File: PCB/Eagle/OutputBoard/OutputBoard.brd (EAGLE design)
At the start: 100 x 80 mm, 10 parts, among them IC1 74LS138N

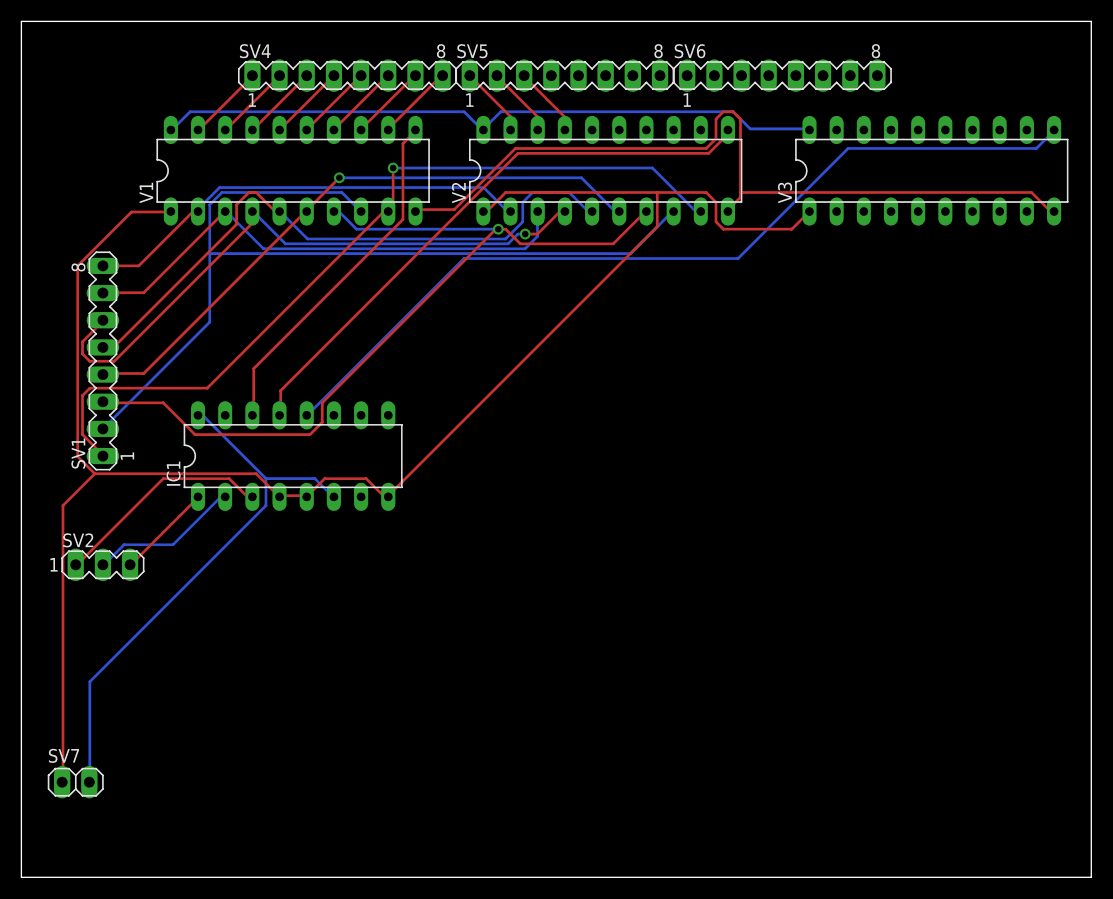
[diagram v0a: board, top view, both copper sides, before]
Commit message: Blank display for IAS and updates in PCB boards
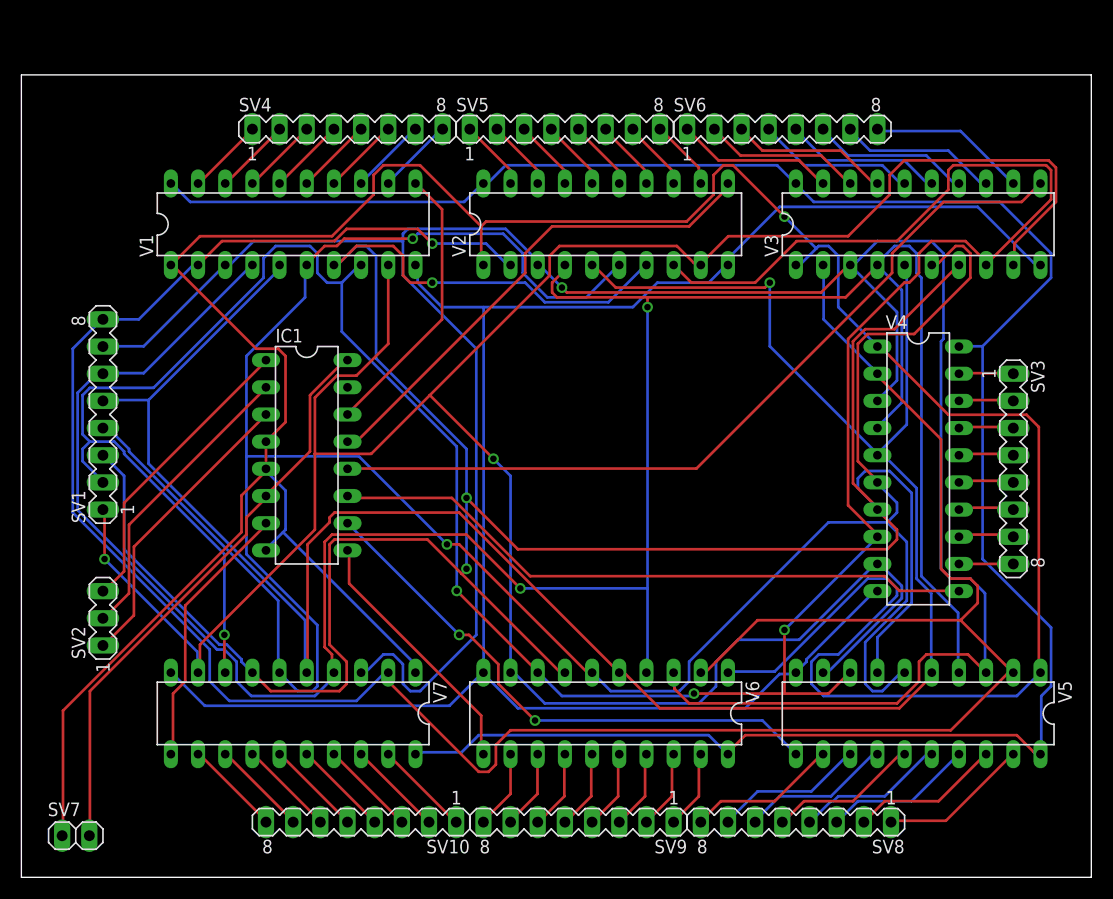
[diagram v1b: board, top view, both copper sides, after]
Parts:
- added SV10, SV3, SV8, SV9: (no value), con-lstb:MA08-1
- added V4, V5, V6, V7: 74574N, 74ttl-din:DIL20
- moved V3 5.16 mm to (83.8, 61.0)
- moved V1 5.00 mm to (25.4, 61.0)
- moved V2 5.00 mm to (54.6, 61.0)
- moved SV1 5.00 mm to (7.62, 43.3)
- moved SV2 5.00 mm to (7.62, 24.2), turned to 90 degrees
- moved SV4 5.00 mm to (30.5, 69.9)
- moved SV5 5.00 mm to (50.8, 69.9)
- moved SV6 5.00 mm to (71.1, 69.9)
- moved SV7 5.00 mm to (5.08, 3.89)
- moved IC1 1.27 mm to (26.7, 39.5), turned to 270 degrees
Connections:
- removed net BUS0: SV1.8, V1.2, V2.2
- removed net DATA4: SV1.4, V1.6, V2.6
- removed net DATA5: SV1.3, V1.7, V2.7
- removed net DATA6: SV1.2, V1.8, V2.8
- removed net DATA7: SV1.1, V1.9, V2.9
- removed net N$13: SV1.7, V1.3, V2.3
- removed net N$14: SV1.6, V1.4, V2.4
- removed net N$15: SV1.5, V1.5, V2.5
- new net BUS1: SV1.8, V1.2, V2.2, V3.2, V4.2, V5.2, V6.2, V7.2
- new net DATA1: SV1.1, V1.9, V2.9, V3.9, V4.9, V5.9, V6.9, V7.9
- new net DATA2: SV1.2, V1.8, V2.8, V3.8, V4.8, V5.8, V6.8, V7.8
- new net DATA3: SV1.3, V1.7, V2.7, V3.7, V4.7, V5.7, V6.7, V7.7
- new net DATA8: SV1.4, V1.6, V2.6, V3.6, V4.6, V5.6, V6.6, V7.6
- new net N$26: IC1.11, V4.11
- new net N$27: IC1.10, V5.11
- new net N$28: IC1.9, V6.11
- new net N$29: SV1.7, V1.3, V2.3, V3.3, V4.3, V5.3, V6.3, V7.3
- new net N$30: SV6.1, V3.19
- new net N$31: SV6.2, V3.18
- new net N$32: SV6.3, V3.17
- new net N$33: SV6.4, V3.16
- new net N$34: SV6.5, V3.15
- new net N$35: SV6.6, V3.14
- new net N$36: SV6.7, V3.13
- new net N$37: SV6.8, V3.12
- new net N$38: SV3.1, V4.19
- new net N$39: SV3.2, V4.18
- new net N$40: SV3.3, V4.17
- new net N$41: SV3.4, V4.16
- new net N$42: SV3.5, V4.15
- new net N$43: SV3.6, V4.14
- new net N$44: SV3.7, V4.13
- new net N$45: SV3.8, V4.12
- new net N$46: SV1.6, V1.4, V2.4, V3.4, V4.4, V5.4, V6.4, V7.4
- new net N$47: SV1.5, V1.5, V2.5, V3.5, V4.5, V5.5, V6.5, V7.5
- new net N$48: SV8.1, V5.19
- new net N$49: SV8.2, V5.18
- new net N$50: SV8.3, V5.17
- new net N$51: SV8.4, V5.16
- new net N$52: SV8.5, V5.15
- new net N$53: SV8.6, V5.14
- new net N$54: SV8.7, V5.13
- new net N$55: SV8.8, V5.12
- new net N$56: SV9.1, V6.19
- new net N$57: SV9.2, V6.18
- new net N$58: SV9.3, V6.17
- new net N$59: SV9.4, V6.16
- new net N$60: SV9.5, V6.15
- new net N$61: SV9.6, V6.14
- new net N$62: SV9.7, V6.13
- new net N$63: SV9.8, V6.12
- new net N$64: IC1.7, V7.11
- new net N$65: SV10.1, V7.19
- new net N$66: SV10.2, V7.18
- new net N$67: SV10.3, V7.17
- new net N$68: SV10.4, V7.16
- new net N$69: SV10.5, V7.15
- new net N$70: SV10.6, V7.14
- new net N$71: SV10.7, V7.13
- new net N$72: SV10.8, V7.12
- net +UB: now also V4.20, V5.20, V6.20, V7.20; no longer V1.20
- net -UB: now also V4.10, V5.10, V6.10, V7.10
- net GND: now also V4.1, V5.1, V6.1, V7.1
- net VCC: now also V1.20
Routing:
- net DATA2: track 0.00 -> 258.5 mm, vias 0 -> 4
- net DATA3: track 0.00 -> 254.2 mm, vias 0 -> 3
- net DATA8: track 0.00 -> 251.5 mm, vias 0 -> 2
- net DATA1: track 0.00 -> 246.7 mm, vias 0 -> 2
- net BUS1: track 0.00 -> 243.9 mm, vias 0 -> 1
- net N$46: track 0.00 -> 243.6 mm, vias 0 -> 2
- net N$29: track 0.00 -> 237.0 mm, vias 0 -> 1
- net N$47: track 0.00 -> 214.8 mm, vias 0 -> 1
- net +UB: track 62.5 -> 203.8 mm
- net GND: track 164.1 -> 284.8 mm, vias 0 -> 1
- net -UB: track 74.8 -> 176.2 mm
- net DATA6: track 85.4 -> 0.00 mm
- net DATA5: track 78.9 -> 0.00 mm, vias 1 -> 0
- net DATA7: track 76.9 -> 0.00 mm, vias 1 -> 0
- net N$26: track 0.00 -> 60.8 mm
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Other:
- board size 100 x 80 mm -> 100 x 75 mm

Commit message: New InputBoard and some modifications to OutputBoard
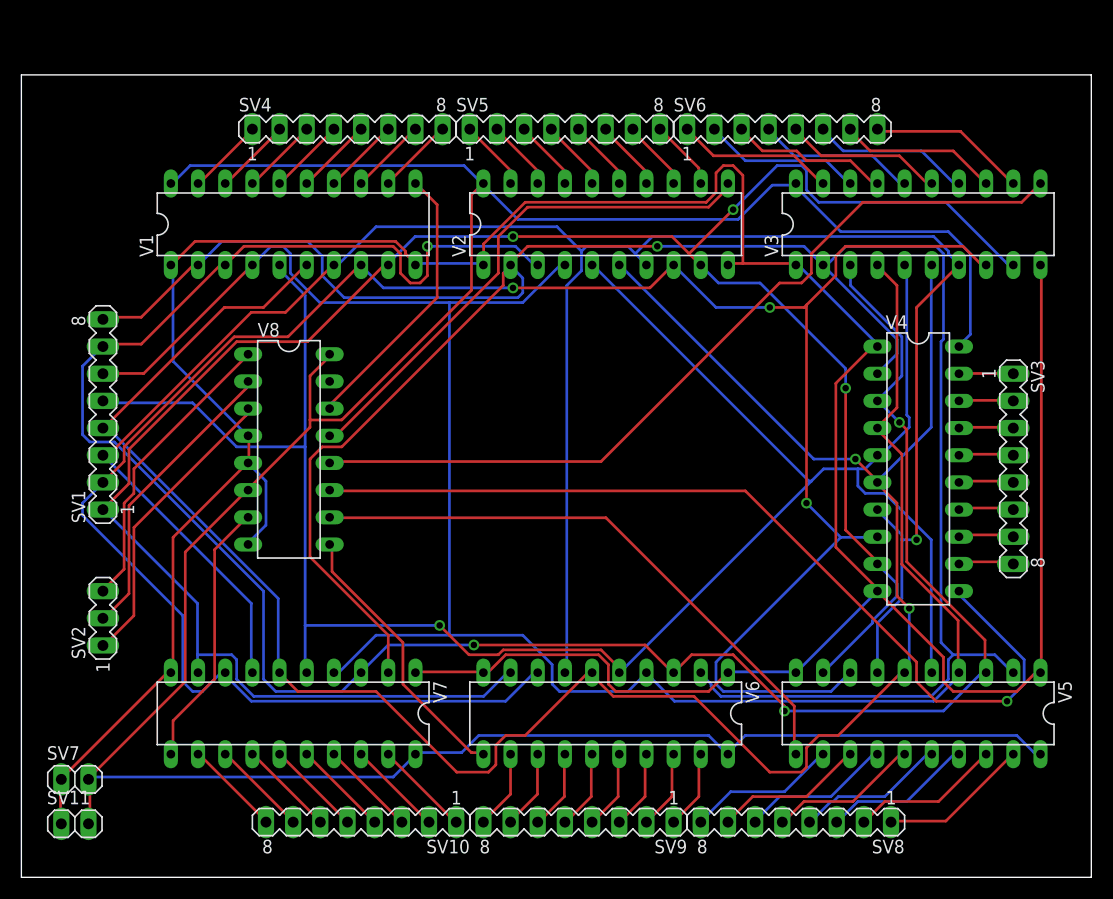
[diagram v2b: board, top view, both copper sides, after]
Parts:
- removed IC1: 74LS138N, 74xx-us:DIL16
- added SV11: (no value), pinhead:1X02
- added V8: 74238N, 74ttl-din:DIL16
- moved SV7 5.27 mm to (5.00, 9.16)
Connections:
- removed net +UB: V2.20, V3.20, V4.20, V5.20, V6.20, V7.20
- removed net -UB: V1.10, V2.10, V3.10, V4.10, V5.10, V6.10, V7.10
- removed net N$21: IC1.2, SV2.2
- removed net N$22: IC1.3, SV2.1
- new net N$13: SV2.2, V8.2
- new net N$14: SV2.1, V8.3
- net GND: now also SV11.1, V1.10, V2.10, V3.10, V4.10, V5.10, V6.10, V7.10, V8.4, V8.5, V8.8; no longer IC1.4, IC1.5, IC1.8
- net N$1: now also V8.12; no longer IC1.12
- net N$20: now also V8.1; no longer IC1.1
- net N$26: now also V8.11; no longer IC1.11
- net N$27: now also V8.10; no longer IC1.10
- net N$28: now also V8.9; no longer IC1.9
- net N$3: now also V8.14; no longer IC1.14
- net N$4: now also V8.13; no longer IC1.13
- net N$64: now also V8.7; no longer IC1.7
- net VCC: now also SV11.2, V2.20, V3.20, V4.20, V5.20, V6.20, V7.20, V8.16, V8.6; no longer IC1.16, IC1.6
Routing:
- net VCC: track 54.7 -> 267.9 mm
- net +UB: track 203.8 -> 0.00 mm
- net -UB: track 176.2 -> 0.00 mm
- net N$46: track 243.6 -> 192.9 mm, vias 2 -> 0
- net DATA3: track 254.2 -> 205.7 mm, vias 3 -> 1
- net DATA8: track 251.5 -> 205.7 mm
- net DATA2: track 258.5 -> 217.9 mm, vias 4 -> 3
- net DATA1: track 246.7 -> 210.9 mm, vias 2 -> 3
- net N$21: track 27.9 -> 0.00 mm
- net N$22: track 27.9 -> 0.00 mm
- net N$13: track 0.00 -> 27.8 mm
- net N$14: track 0.00 -> 27.8 mm
- net N$26: track 60.8 -> 86.1 mm, vias 0 -> 1
- net N$29: track 237.0 -> 211.9 mm, vias 1 -> 4
- net N$47: track 214.8 -> 195.7 mm
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
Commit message: PCB Modified with proper flip flop 74 273 and ground fill
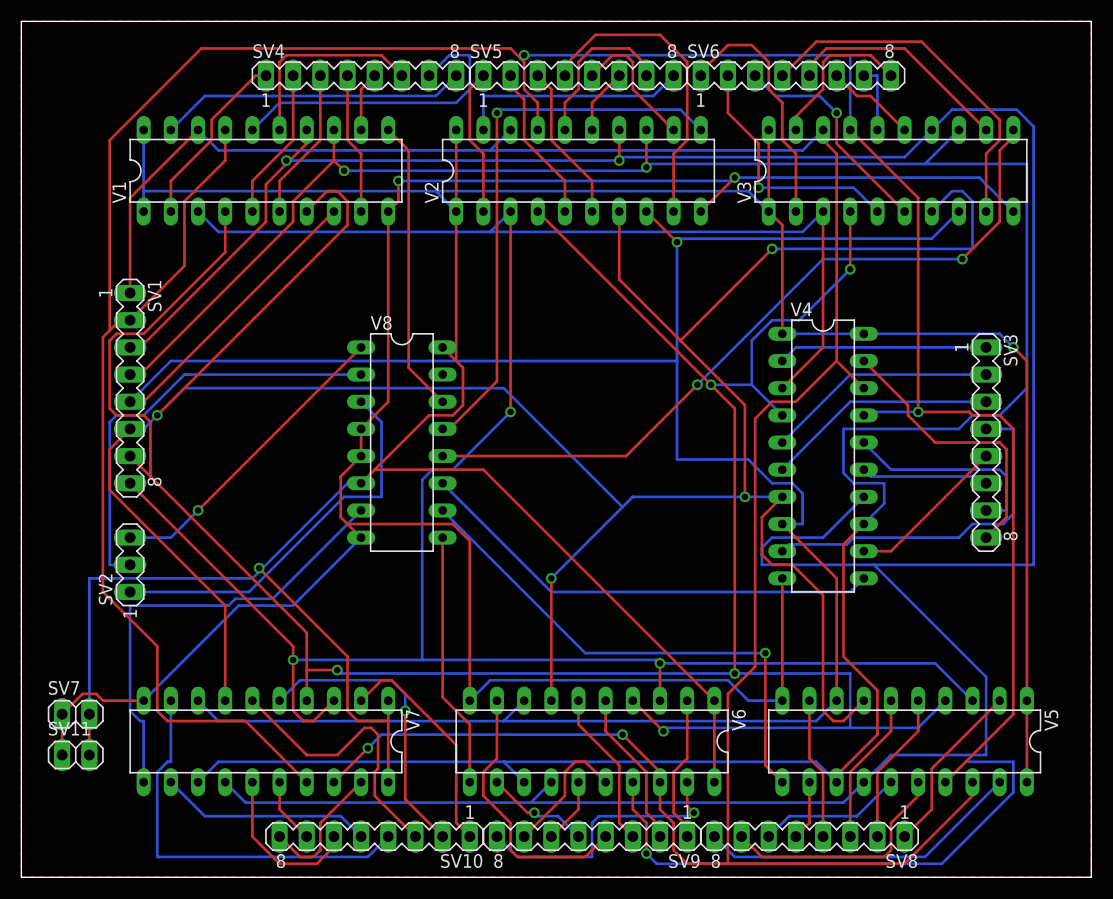
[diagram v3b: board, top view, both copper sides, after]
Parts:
- V1, V2, V3, V4, V5, V6, V7: value 74574N -> 74273N
- moved V8 10.6 mm to (35.6, 40.6)
- moved V4 8.97 mm to (74.9, 39.4)
- moved SV11 6.43 mm to (5.08, 11.4)
- moved SV7 6.08 mm to (5.08, 15.2)
- moved V1 5.61 mm to (22.9, 66.0)
- moved V2 5.61 mm to (52.1, 66.0)
- moved V3 5.61 mm to (81.3, 66.0)
- moved SV2 5.61 mm to (10.2, 29.2)
- moved SV5 5.16 mm to (52.1, 74.9)
- moved SV4 5.16 mm to (31.8, 74.9)
- moved SV6 5.16 mm to (72.4, 74.9)
- moved V7 3.65 mm to (22.9, 12.7)
- moved SV1 3.54 mm to (10.2, 45.7), turned to 270 degrees
- moved SV3 3.54 mm to (90.2, 40.6)
- moved V5 2.91 mm to (82.5, 12.7)
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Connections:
- net BUS1: now also V1.3, V2.3, V3.3, V4.3, V5.3, V6.3, V7.3; no longer V1.2, V2.2, V3.2, V4.2, V5.2, V6.2, V7.2
- net DATA1: now also V1.18, V2.18, V3.18, V4.18, V5.18, V6.18, V7.18; no longer V1.9, V2.9, V3.9, V4.9, V5.9, V6.9, V7.9
- net DATA2: now also V1.17, V2.17, V3.17, V4.17, V5.17, V6.17, V7.17; no longer V1.8, V2.8, V3.8, V4.8, V5.8, V6.8, V7.8
- net DATA3: now also V1.14, V2.14, V3.14, V4.14, V5.14, V6.14, V7.14; no longer V1.7, V2.7, V3.7, V4.7, V5.7, V6.7, V7.7
- net DATA8: now also V1.13, V2.13, V3.13, V4.13, V5.13, V6.13, V7.13; no longer V1.6, V2.6, V3.6, V4.6, V5.6, V6.6, V7.6
- net GND: no longer V1.1, V2.1, V3.1, V4.1, V5.1, V6.1, V7.1
- net N$10: now also V1.16; no longer V1.13
- net N$11: now also V1.19; no longer V1.12
- net N$12: now also V2.2; no longer V2.19
- net N$16: now also V2.5; no longer V2.18
- net N$17: now also V2.6; no longer V2.17
- net N$18: now also V2.9; no longer V2.16
- net N$19: now also V2.12; no longer V2.15
- net N$2: now also V1.2; no longer V1.19
- net N$23: now also V2.15; no longer V2.14
- net N$24: now also V2.16; no longer V2.13
- net N$25: now also V2.19; no longer V2.12
- net N$29: now also V1.4, V2.4, V3.4, V4.4, V5.4, V6.4, V7.4; no longer V1.3, V2.3, V3.3, V4.3, V5.3, V6.3, V7.3
- net N$30: now also V3.2; no longer V3.19
- net N$31: now also V3.5; no longer V3.18
- net N$32: now also V3.6; no longer V3.17
- net N$33: now also V3.9; no longer V3.16
- net N$34: now also V3.12; no longer V3.15
- net N$35: now also V3.15; no longer V3.14
- net N$36: now also V3.16; no longer V3.13
- net N$37: now also V3.19; no longer V3.12
- net N$38: now also V4.2; no longer V4.19
- net N$39: now also V4.5; no longer V4.18
- net N$40: now also V4.6; no longer V4.17
- net N$41: now also V4.9; no longer V4.16
- net N$42: now also V4.12; no longer V4.15
- net N$43: now also V4.15; no longer V4.14
- net N$44: now also V4.16; no longer V4.13
- net N$45: now also V4.19; no longer V4.12
- net N$46: now also V1.7, V2.7, V3.7, V4.7, V5.7, V6.7, V7.7; no longer V1.4, V2.4, V3.4, V4.4, V5.4, V6.4, V7.4
- net N$47: now also V1.8, V2.8, V3.8, V4.8, V5.8, V6.8, V7.8; no longer V1.5, V2.5, V3.5, V4.5, V5.5, V6.5, V7.5
- net N$48: now also V5.2; no longer V5.19
- net N$49: now also V5.5; no longer V5.18
- net N$5: now also V1.5; no longer V1.18
- net N$50: now also V5.6; no longer V5.17
- net N$51: now also V5.9; no longer V5.16
- net N$52: now also V5.12; no longer V5.15
- net N$53: now also V5.15; no longer V5.14
- net N$54: now also V5.16; no longer V5.13
- net N$55: now also V5.19; no longer V5.12
- net N$56: now also V6.2; no longer V6.19
- net N$57: now also V6.5; no longer V6.18
- net N$58: now also V6.6; no longer V6.17
- net N$59: now also V6.9; no longer V6.16
- net N$6: now also V1.6; no longer V1.17
- net N$60: now also V6.12; no longer V6.15
- net N$61: now also V6.15; no longer V6.14
- net N$62: now also V6.16; no longer V6.13
- net N$63: now also V6.19; no longer V6.12
- net N$65: now also V7.2; no longer V7.19
- net N$66: now also V7.5; no longer V7.18
- net N$67: now also V7.6; no longer V7.17
- net N$68: now also V7.9; no longer V7.16
- net N$69: now also V7.12; no longer V7.15
- net N$7: now also V1.9; no longer V1.16
- net N$70: now also V7.15; no longer V7.14
- net N$71: now also V7.16; no longer V7.13
- net N$72: now also V7.19; no longer V7.12
- net N$8: now also V1.12; no longer V1.15
- net N$9: now also V1.15; no longer V1.14
- net VCC: now also V1.1, V2.1, V3.1, V4.1, V5.1, V6.1, V7.1
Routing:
- net DATA2: track 217.9 -> 317.8 mm
- net GND: track 295.9 -> 208.1 mm, vias 0 -> 2
- net DATA3: track 205.7 -> 281.4 mm, vias 1 -> 2
- net N$46: track 192.9 -> 252.5 mm, vias 0 -> 4
- net VCC: track 267.9 -> 315.5 mm, vias 0 -> 2
- net DATA8: track 205.7 -> 249.1 mm
- net N$26: track 86.1 -> 44.1 mm, vias 1 -> 0
- net N$47: track 195.7 -> 231.4 mm
- net N$68: track 8.98 -> 37.7 mm
- net N$41: track 5.14 -> 33.5 mm
- net N$18: track 6.64 -> 29.1 mm
- net N$10: track 7.22 -> 29.7 mm
- net DATA1: track 210.9 -> 232.7 mm, vias 3 -> 2
- net N$11: track 7.24 -> 28.8 mm
- net N$45: track 5.29 -> 26.4 mm
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- added copper zone on layer 16, net GND
- added copper zone on layer 1, net VCC
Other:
- board size 100 x 75 mm -> 100 x 80 mm
